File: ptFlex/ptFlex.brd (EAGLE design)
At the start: 67.3 x 88.9 mm, 64 parts, among them J1 5.5x2.1mm Barrel, Q1 BSS138, Q2 2N2222, U2 UBLOX_MAX, U3 LM1086, U4 RADIOMETRIX-HX1-CUSTOM, U5 LP3985IM5-3.3/NOPB, U6 MCP6L01T, U7 ATMega328, U8 BME280, X1 BU-SMA-H, Y1 16MHz

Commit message: Added GPS filter
Version 1.04
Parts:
- added F1: MURATA-GPS-FILTER, custom-ds:MURATA-GPS-FILTER
- moved ANT1 4.77 mm to (63.5, 51.4)
- renumbered SV1 to J3, SV2 to J4, SV3 to J2
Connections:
- removed net N$16: ANT1.FEED, U2.11_RF_IN
- new net N$2: F1.P$1, U2.11_RF_IN
- new net N$3: ANT1.FEED, F1.P$3
- net GND: now also F1.P$2, F1.P$4
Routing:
- net N$3: track 0.00 -> 3.79 mm
- net N$2: track 0.00 -> 3.70 mm
- net N$16: track 3.58 -> 0.00 mm
- net GND: vias 69 -> 71
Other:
- outline, holes or cut-outs redrawn
- board text added: "Project: Traveler ptFlex v1.04 Custom Digital Services, LLC www.custom-ds.com"
- board text added: "Qwiic"
- board text removed: "Project: Traveler ptFlex v1.03 Custom Digital Services, LLC www.custom-ds.com"

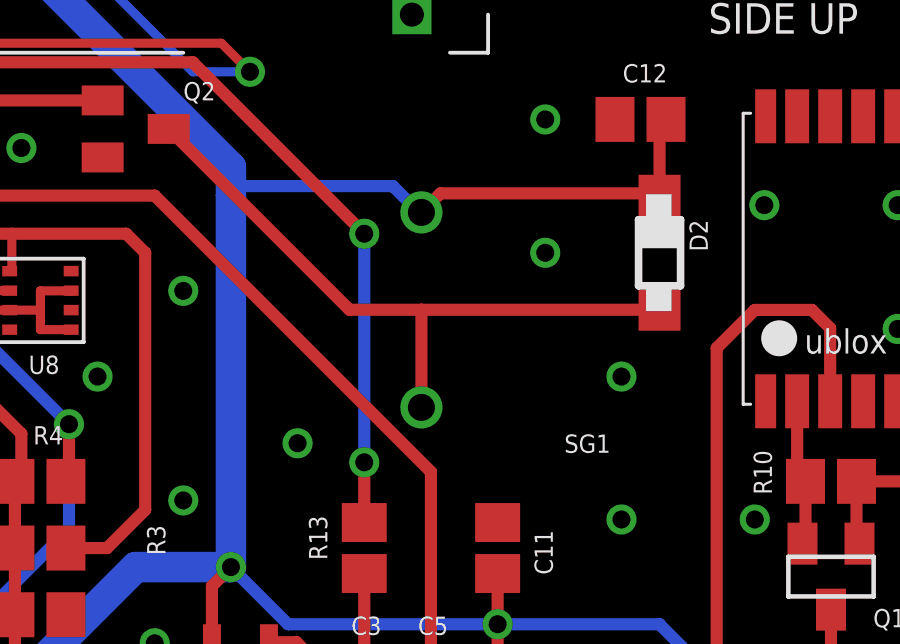
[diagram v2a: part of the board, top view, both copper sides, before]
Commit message: Minor tweak to piezo to open up ground plane
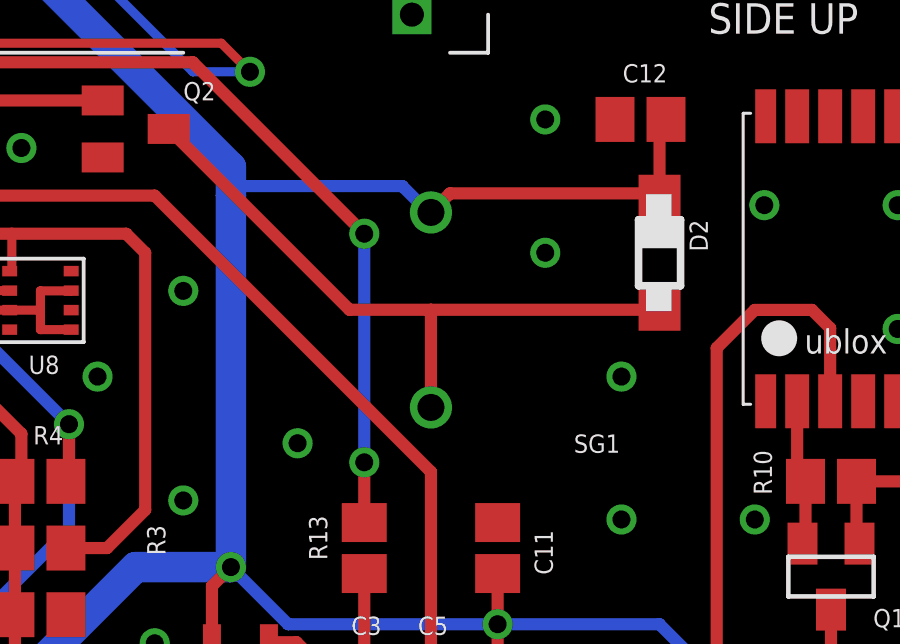
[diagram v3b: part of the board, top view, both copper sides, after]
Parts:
- moved SG1 0.32 mm to (45.4, 37.1)
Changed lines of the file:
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@@
 <setting verticaltext="up"/>
 </settings>
-<grid distance="0.0125" unitdist="inch" unit="inch" style="lines" multiple="1" display="no" altdistance="0.00625" altunitdist="inch" altunit="inch"/>
+<grid distance="0.0125" unitdist="inch" unit="inch" style="lines" multiple="1" display="yes" altdistance="0.00625" altunitdist="inch" altunit="inch"/>
 <layers>
 <layer number="1" name="Top" color="4" fill="1" visible="yes" active="yes"/>
@@
 <attribute name="DIGIKEY" value="311-1361-1-ND" x="15.5575" y="20.955" size="1.778" layer="27" display="off"/>
 </element>
-<element name="SG1" library="SparkFun-Electromechanical" package="BUZZER-12MM-NS" value="BUZZERNS" x="45.085" y="37.1475" smashed="yes" rot="R90">
-<attribute name="NAME" x="49.8475" y="32.385" size="0.6096" layer="25" font="vector" ratio="10"/>
-<attribute name="VALUE" x="48.133" y="33.9725" size="0.6096" layer="27" ratio="10" rot="R90"/>
-<attribute name="DIGIKEY" value="102-1155-ND" x="45.085" y="37.1475" size="1.778" layer="27" rot="R90" display="off"/>
+<element name="SG1" library="SparkFun-Electromechanical" package="BUZZER-12MM-NS" value="BUZZERNS" x="45.4025" y="37.1475" smashed="yes" rot="R90">
+<attribute name="NAME" x="50.165" y="32.385" size="0.6096" layer="25" font="vector" ratio="10"/>
+<attribute name="VALUE" x="48.4505" y="33.9725" size="0.6096" layer="27" ratio="10" rot="R90"/>
+<attribute name="DIGIKEY" value="102-1155-ND" x="45.4025" y="37.1475" size="1.778" layer="27" rot="R90" display="off"/>
 </element>
 <element name="C3" library="resistor" package="C0805" value=".1uF" x="43.18" y="24.13" smashed="yes" rot="R90">
@@
 <wire x1="8.5725" y1="21.59" x2="12.3825" y2="21.59" width="0.4064" layer="1"/>
 <wire x1="52.9425" y1="41.0325" x2="53.0225" y2="40.9525" width="0.4064" layer="1"/>
-<wire x1="52.9425" y1="41.0325" x2="45.72" y2="41.0325" width="0.4064" layer="1"/>
-<wire x1="45.72" y1="41.0325" x2="45.085" y2="40.3975" width="0.4064" layer="1"/>
-<wire x1="45.085" y1="40.3975" x2="45.01" y2="40.3975" width="0.4064" layer="16"/>
-<wire x1="45.01" y1="40.3975" x2="44.1325" y2="41.275" width="0.4064" layer="16"/>
-<wire x1="44.1325" y1="41.275" x2="39.0525" y2="41.275" width="0.4064" layer="16"/>
+<wire x1="52.9425" y1="41.0325" x2="46.0375" y2="41.0325" width="0.4064" layer="1"/>
+<wire x1="46.0375" y1="41.0325" x2="45.4025" y2="40.3975" width="0.4064" layer="1"/>
+<wire x1="45.4025" y1="40.3975" x2="45.3275" y2="40.3975" width="0.4064" layer="16"/>
+<wire x1="45.3275" y1="40.3975" x2="44.45" y2="41.275" width="0.4064" layer="16"/>
+<wire x1="44.45" y1="41.275" x2="39.0525" y2="41.275" width="0.4064" layer="16"/>
 <wire x1="39.0525" y1="41.275" x2="38.735" y2="40.9575" width="0.4064" layer="16"/>
 </signal>
@@
 <contactref element="D2" pad="A"/>
 <wire x1="36.66" y1="43.18" x2="36.66" y2="43.0325" width="0.4064" layer="1"/>
-<wire x1="53.0225" y1="37.1525" x2="45.085" y2="37.1525" width="0.4064" layer="1"/>
-<wire x1="45.085" y1="37.1525" x2="42.6875" y2="37.1525" width="0.4064" layer="1"/>
+<wire x1="53.0225" y1="37.1525" x2="45.4025" y2="37.1525" width="0.4064" layer="1"/>
+<wire x1="45.4025" y1="37.1525" x2="42.6875" y2="37.1525" width="0.4064" layer="1"/>
 <wire x1="42.6875" y1="37.1525" x2="36.66" y2="43.18" width="0.4064" layer="1"/>
-<wire x1="45.085" y1="33.8975" x2="45.085" y2="37.1525" width="0.4064" layer="1"/>
+<wire x1="45.4025" y1="33.8975" x2="45.4025" y2="37.1525" width="0.4064" layer="1"/>
 </signal>
 <signal name="N$13">

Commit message: Final check in for hardware version 1
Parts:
- removed L4, L5, L6, L7: 160 ohm, inductor-neosid:SM-1206
- removed U4: RADIOMETRIX-HX1-CUSTOM, custom-ds:RADIOMETRIX-HX1-CUSTOM
- added C18, C19, C20, C21: .1uF, resistor:C0805
- added D4: LL4148, custom-ds:SOD-80
- added Q3: BSS138, SparkFun-DiscreteSemi:SOT23
- added R18, R19, R20, R21, R22, R23, R24, R25, R26: 10k, resistor:R0805
- added U1: DRA818V, custom-ds:SMD_DRA818
- L1, L2, L3: value 160 ohm -> 1µH; device inductor-neosid:SM-1206 -> custom-ds:L0805
- moved R6 51.5 mm to (50.5, 47.9), turned to 270 degrees
- moved LED2 39.3 mm to (46.4, 47.9)
- moved LED1 39.0 mm to (42.9, 47.9)
- moved C13 33.6 mm to (26.4, 49.5)
- moved R5 32.7 mm to (39.1, 47.9), turned to 90 degrees
- moved C4 25.8 mm to (41.0, 70.5), turned to 0 degrees
- moved L1 14.6 mm to (7.94, 74.9), turned to 0 degrees
- moved L3 14.3 mm to (17.8, 74.9), turned to 0 degrees
- moved L2 6.07 mm to (13.7, 74.9), turned to 0 degrees
- moved C1 0.63 mm to (16.2, 21.0)
- moved D1 0.63 mm to (2.54, 13.7)
- moved R2 0.63 mm to (5.08, 14.6)
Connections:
- removed net N$23: LED1.A, R5.2
- removed net RFGND: U4.ANTENNA_GND1, U4.ANTENNA_GND2, X1.2, X1.3, X1.4, X1.5
- removed net VCC: L7.1, U4.VCC
- new net N$16: R19.1, R20.2, U1.6
- new net N$21: LED1.C, R5.2
- new net N$28: R26.1, U1.16
- new net N$6: C18.1, L1.1, U1.12
- net +5V: now also D4.ANODE, LED1.A, R24.2; no longer L7.2
- net DIG-PTT: now also R18.1; no longer L1.2
- net DIG-XMIT-PS: now also R20.1; no longer L2.1
- net GND: now also C18.2, C19.2, C20.2, C21.2, R19.2, R21.2, R22.2, R23.1, U1.10, U1.9, X1.2, X1.3, X1.4, X1.5; no longer LED1.C, U4.GND
- net N$10: now also U1.18; no longer L4.2
- net N$12: now also D4.CATHODE, Q3.1, R25.2, U1.8; no longer L5.2, U4.RX_AUDIO
- net N$14: now also R18.2, R21.1, U1.5; no longer L2.2, U4.POWER_SAVE
- net N$19: now also R22.1, U1.7; no longer L6.2, U4.RX_DATA
- net N$20: now also Q3.2, R25.1, U1.17; no longer L3.2, U4.TX_DATA
- net N$4: now also C20.1, L2.2, L3.1; no longer U4.ANTENNA, X1.1
- net N$5: now also C19.1, L1.2, L2.1; no longer L4.1, U4.TX_AUDIO
- net N$7: now also C21.1, L3.2, X1.1; no longer L1.1, U4.PTT
- net RX-AUDIO: now also U1.3; no longer L5.1
- net XCEIVER-RX: now also R23.2, R26.2; no longer L3.1
- net XCEIVER-TX: now also Q3.3, R24.1; no longer L6.1
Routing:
- net +5V: track 237.7 -> 71.7 mm, vias 7 -> 8
- net N$25: track 90.9 -> 4.62 mm, vias 4 -> 0
- net N$10: track 85.0 -> 9.63 mm, vias 4 -> 2
- net XCEIVER-RX: track 64.9 -> 0.00 mm, vias 2 -> 0
- net XCEIVER-TX: track 64.5 -> 0.00 mm, vias 2 -> 0
- net DIG-XMIT-PS: track 65.1 -> 6.91 mm, vias 2 -> 1
- net RX-AUDIO: track 92.1 -> 36.9 mm, vias 2 -> 1
- net DIG-PTT: track 57.8 -> 13.2 mm, vias 2 -> 1
- net ANA-RX-AUD: track 48.0 -> 37.5 mm
- net N$4: track 8.25 -> 0.00 mm
- net SCK: track 24.8 -> 16.7 mm
- net N$23: track 6.24 -> 0.00 mm
- net N$12: track 2.48 -> 8.29 mm
- net N$21: track 0.00 -> 4.18 mm
- net VCC: track 2.48 -> 0.00 mm
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- added copper zone on layer 2, net +5V
- added copper zone on layer 15, net GND
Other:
- board text added: "Project: Traveler ptFlex v2.00 Custom Digital Services, LLC www.custom-ds.com"
- board text removed: "Project: Traveler ptFlex v1.04 Custom Digital Services, LLC www.custom-ds.com"
